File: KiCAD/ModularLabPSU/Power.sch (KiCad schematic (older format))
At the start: 22 parts, among them K1 HF115F, P2 CONN_01X06, Q3 BC847B, Q4 BC847B, U10 LM317_SOT223, U11 LM317AT, U9 LM317HVT

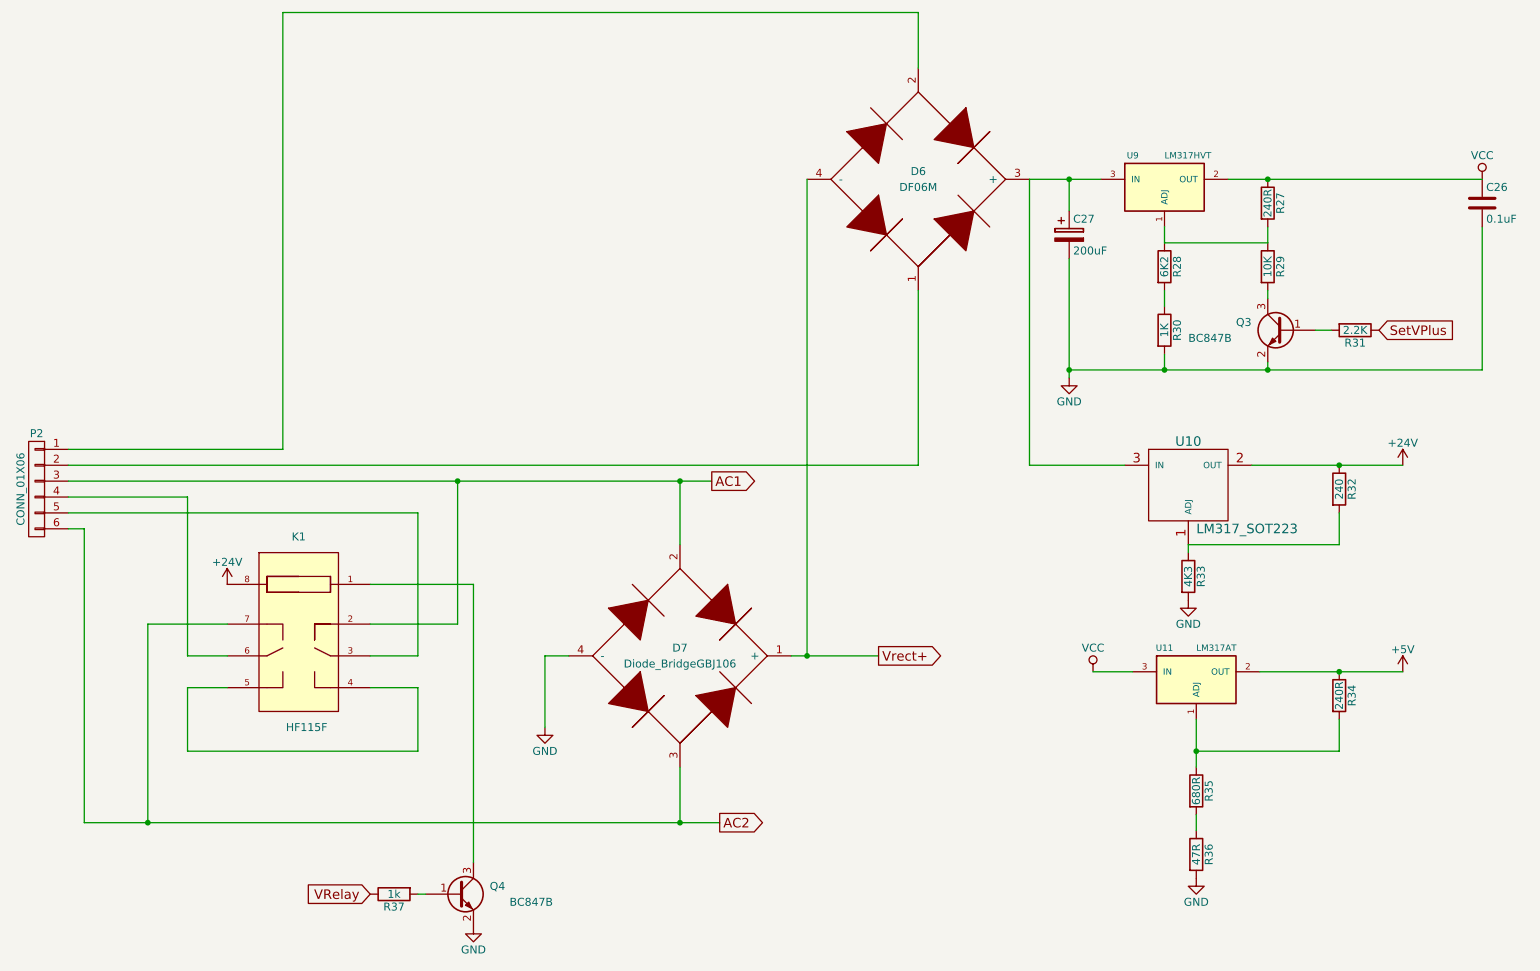
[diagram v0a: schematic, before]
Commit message: Started re-design of PCB. Schematic changes from testing first board and started developing new layout
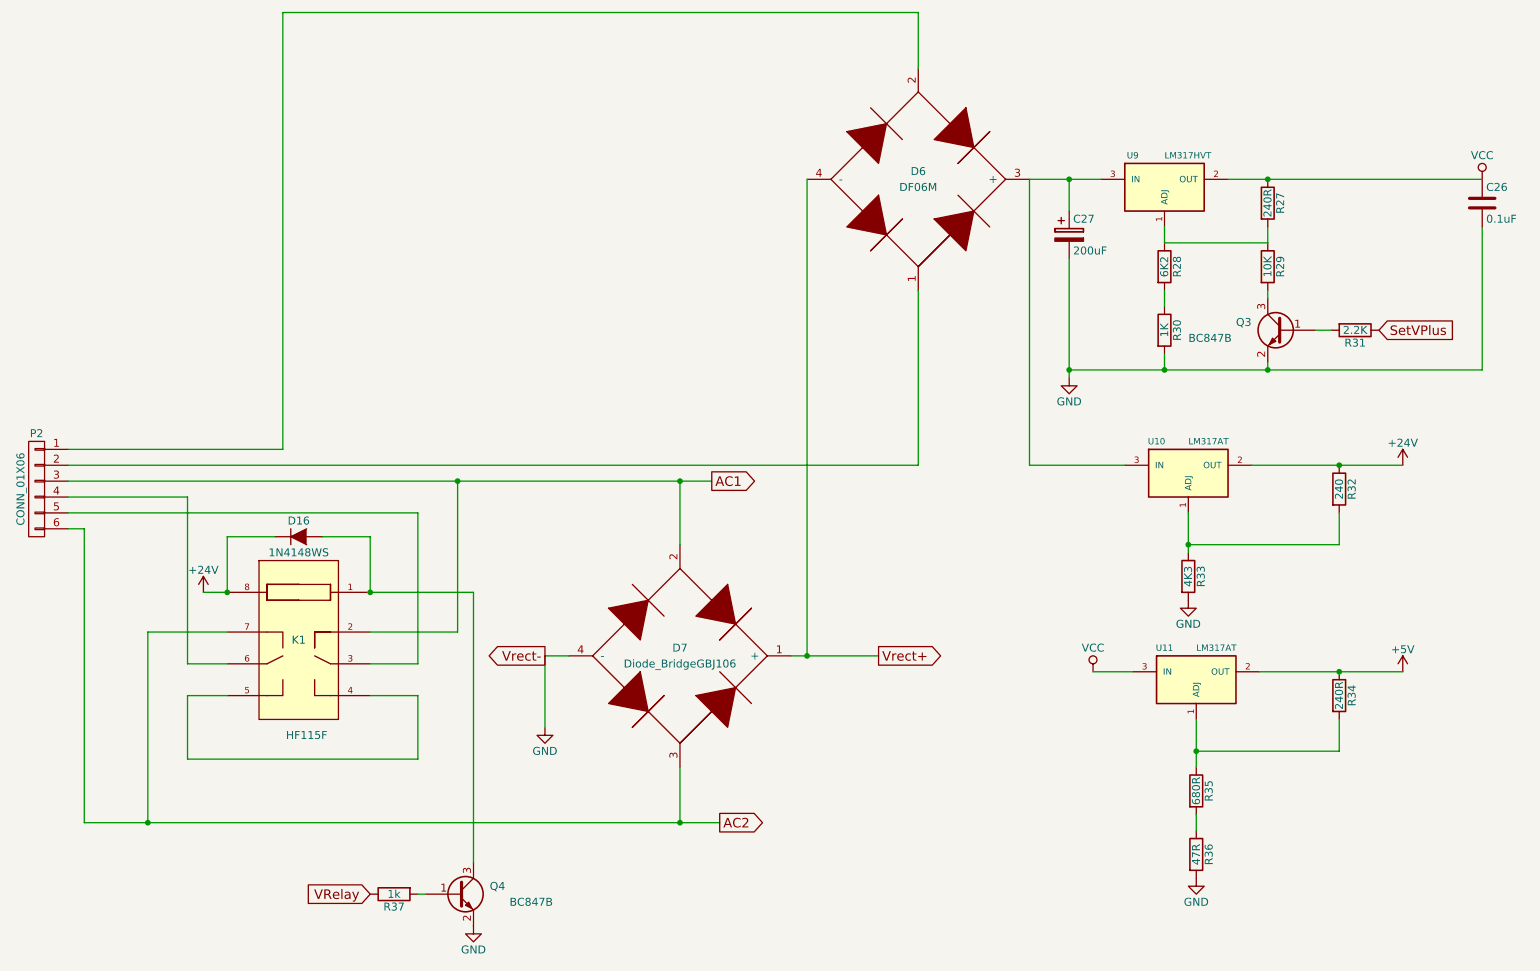
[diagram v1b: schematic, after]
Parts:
- removed U10: LM317_SOT223, ab2_sot:AB2_SOT223, symbol LM317_SOT223
- added D16: 1N4148WS, Diodes_SMD:SOD-323, symbol D
- added U10: LM317AT, Power_Integrations:TO-220, symbol LM317AT
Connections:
- net +24V: now also D16.1 (K), U10.2 (OUT)
- net at C27.1, D6.3 (+), U9.3 (IN): now also U10.3 (IN)
- net at R32.2, R33.1: now also U10.1 (ADJ)
- net at K1.1, Q4.3 (C): now also D16.2 (A)
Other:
- moved on the sheet: K1
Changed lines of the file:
@@
 EESchema Schematic File Version 2
+LIBS:VCS1625
+LIBS:ModularLabPSU-rescue
+LIBS:ceramicResonator
+LIBS:diode_bridge_df06m
+LIBS:diode_bridge_GBJ1506
+LIBS:hf115f
+LIBS:ad780brz
+LIBS:ad5689
+LIBS:ad7705bruz
+LIBS:adum1201arz-rl7
+LIBS:custompower
+LIBS:LM317HVT
+LIBS:LT1639
+LIBS:LT1716
+LIBS:LTC2050
+LIBS:MCP2200
+LIBS:MCR100
+LIBS:MOLEXusb_mini_b_otg
+LIBS:OMRON G2RL-24-CF-DC24
 LIBS:power
 LIBS:device
@@
 LIBS:contrib
 LIBS:valves
-LIBS:ad780brz
-LIBS:ad5689
-LIBS:ad7705bruz
-LIBS:adum1201arz-rl7
-LIBS:ceramicResonator
-LIBS:custompower
-LIBS:diode_bridge_df06m
-LIBS:diode_bridge_GBJ1506
-LIBS:hf115f
-LIBS:LM317HVT
-LIBS:LT1639
-LIBS:LT1716
-LIBS:LTC2050
-LIBS:MCP2200
-LIBS:MCR100
 LIBS:ModularLabPSU-cache
-LIBS:ModularLabPSU-rescue
-LIBS:MOLEXusb_mini_b_otg
-LIBS:OMRON G2RL-24-CF-DC24
 EELAYER 25 0
 EELAYER END
@@
 $EndComp
 $Comp
-L +24V #PWR075
+L +24V #PWR074
 U 1 1 5624A7FF
-P 2400 4350
-F 0 "#PWR075" H 2400 4200 50  0001 C CNN
-F 1 "+24V" H 2400 4490 50  0000 C CNN
-F 2 "" H 2400 4350 60  0000 C CNN
-F 3 "" H 2400 4350 60  0000 C CNN
-	1    2400 4350
+P 2250 4400
+F 0 "#PWR074" H 2250 4250 50  0001 C CNN
+F 1 "+24V" H 2250 4540 50  0000 C CNN
+F 2 "" H 2250 4400 60  0000 C CNN
+F 3 "" H 2250 4400 60  0000 C CNN
+	1    2250 4400
 	1    0    0    -1
 $EndComp
@@
 	1400 3800 2150 3800
 Wire Wire Line
-	2150 3800 2150 4800
-Wire Wire Line
-	2150 4800 2400 4800
-Wire Wire Line
-	1400 3900 3600 3900
-Wire Wire Line
-	3600 3900 3600 4800
-Wire Wire Line
-	3600 4800 3300 4800
-Wire Wire Line
-	2400 5000 2150 5000
-Wire Wire Line
-	2150 5000 2150 5400
-Wire Wire Line
-	2150 5400 3600 5400
-Wire Wire Line
-	3600 5400 3600 5000
-Wire Wire Line
-	3600 5000 3300 5000
-Wire Wire Line
-	2400 4600 1900 4600
-Wire Wire Line
-	1900 4600 1900 5850
+	2150 3800 2150 4850
+Wire Wire Line
+	2150 4850 2400 4850
+Wire Wire Line
+	3600 3900 3600 4850
+Wire Wire Line
+	3600 4850 3300 4850
+Wire Wire Line
+	2400 5050 2150 5050
+Wire Wire Line
+	2150 5450 3600 5450
+Wire Wire Line
+	3600 5450 3600 5050
+Wire Wire Line
+	3600 5050 3300 5050
+Wire Wire Line
+	2400 4650 1900 4650
 Connection ~ 1900 5850
 Wire Wire Line
-	3300 4600 3850 4600
-Wire Wire Line
-	3850 4600 3850 3700
+	3850 4650 3300 4650
+Wire Wire Line
+	3850 3700 3850 4650
 Connection ~ 3850 3700
 $Comp
-L GND #PWR076
+L GND #PWR075
 U 1 1 5624AA06
 P 3950 6500
-F 0 "#PWR076" H 3950 6250 50  0001 C CNN
+F 0 "#PWR075" H 3950 6250 50  0001 C CNN
 F 1 "GND" H 3950 6350 50  0000 C CNN
 F 2 "" H 3950 6500 60  0000 C CNN
@@
 	-1   0    0    -1
 $EndComp
-Wire Wire Line
-	3950 4350 3950 6100
 $Comp
 L R R37
@@
 Connection ~ 5250 5850
 Wire Wire Line
-	3300 4350 3950 4350
+	3300 4400 3950 4400
 Wire Wire Line
 	4550 4800 4400 4800
@@
 	6750 3600 6750 2500
 $Comp
-L GND #PWR077
+L GND #PWR076
 U 1 1 5624D678
 P 4400 5250
-F 0 "#PWR077" H 4400 5000 50  0001 C CNN
+F 0 "#PWR076" H 4400 5000 50  0001 C CNN
 F 1 "GND" H 4400 5100 50  0000 C CNN
 F 2 "" H 4400 5250 60  0000 C CNN
@@
 	7700 2300 7700 3050
 $Comp
-L GND #PWR078
+L GND #PWR077
 U 1 1 5624DFFE
 P 7700 3050
-F 0 "#PWR078" H 7700 2800 50  0001 C CNN
+F 0 "#PWR077" H 7700 2800 50  0001 C CNN
 F 1 "GND" H 7700 2900 50  0000 C CNN
 F 2 "" H 7700 3050 60  0000 C CNN
@@
 	9250 2750 9350 2750
 $Comp
-L VCC #PWR079
+L VCC #PWR078
 U 1 1 5624E69D
 P 10300 1800
-F 0 "#PWR079" H 10300 1650 50  0001 C CNN
+F 0 "#PWR078" H 10300 1650 50  0001 C CNN
 F 1 "VCC" H 10300 1950 50  0000 C CNN
 F 2 "" H 10300 1800 60  0000 C CNN
@@
 	8500 5800 8500 5900
 $Comp
-L GND #PWR080
+L GND #PWR079
 U 1 1 5624F186
 P 8500 6200
-F 0 "#PWR080" H 8500 5950 50  0001 C CNN
+F 0 "#PWR079" H 8500 5950 50  0001 C CNN
 F 1 "GND" H 8500 6050 50  0000 C CNN
 F 2 "" H 8500 6200 60  0000 C CNN
@@
 	7850 4900 8100 4900
 $Comp
-L VCC #PWR081
+L VCC #PWR080
 U 1 1 5624F202
 P 7850 4900
-F 0 "#PWR081" H 7850 4750 50  0001 C CNN
+F 0 "#PWR080" H 7850 4750 50  0001 C CNN
 F 1 "VCC" H 7850 5050 50  0000 C CNN
 F 2 "" H 7850 4900 60  0000 C CNN
@@
 $EndComp
 $Comp
-L +5V #PWR082
+L +5V #PWR081
 U 1 1 5624F229
 P 9800 4900
-F 0 "#PWR082" H 9800 4750 50  0001 C CNN
+F 0 "#PWR081" H 9800 4750 50  0001 C CNN
 F 1 "+5V" H 9800 5040 50  0000 C CNN
 F 2 "" H 9800 4900 60  0000 C CNN
 F 3 "" H 9800 4900 60  0000 C CNN
 	1    9800 4900
-	1    0    0    -1
-$EndComp
-$Comp
-L LM317_SOT223 U10
-U 1 1 5625142C
-P 8450 3750
-F 0 "U10" H 8450 4050 60  0000 C CNN
-F 1 "LM317_SOT223" H 8500 3500 60  0000 L CNN
-F 2 "ab2_sot:AB2_SOT223" H 8450 3750 60  0001 C CNN
-F 3 "" H 8450 3750 60  0000 C CNN
-	1    8450 3750
 	1    0    0    -1
 $EndComp
@@
 	9400 4100 8450 4100
 Wire Wire Line
-	8450 4100 8450 4150
-$Comp
-L GND #PWR083
+	8450 3900 8450 4150
+$Comp
+L GND #PWR082
 U 1 1 56252E95
 P 8450 4450
-F 0 "#PWR083" H 8450 4200 50  0001 C CNN
+F 0 "#PWR082" H 8450 4200 50  0001 C CNN
 F 1 "GND" H 8450 4300 50  0000 C CNN
 F 2 "" H 8450 4450 60  0000 C CNN
@@
 Connection ~ 9400 3600
 $Comp
-L +24V #PWR084
+L +24V #PWR083
 U 1 1 56252F21
 P 9800 3600
-F 0 "#PWR084" H 9800 3450 50  0001 C CNN
+F 0 "#PWR083" H 9800 3450 50  0001 C CNN
 F 1 "+24V" H 9800 3740 50  0000 C CNN
 F 2 "" H 9800 3600 60  0000 C CNN
@@
 L HF115F K1
 U 1 1 562793EF
-P 2850 4650
-F 0 "K1" H 2850 5250 50  0000 C CNN
-F 1 "HF115F" H 2900 4050 50  0000 C CNN
-F 2 "hf115F:HF115F" H 3000 4900 60  0001 C CNN
-F 3 "" H 3000 4900 60  0000 C CNN
-	1    2850 4650
+P 2850 4700
+F 0 "K1" H 2850 4700 50  0000 C CNN
+F 1 "HF115F" H 2900 4100 50  0000 C CNN
+F 2 "hf115F:HF115F" H 3000 4950 60  0001 C CNN
+F 3 "" H 3000 4950 60  0000 C CNN
+	1    2850 4700
 	1    0    0    -1
 $EndComp
@@
 	8900 4900 9800 4900
 Connection ~ 8500 5400
+Wire Wire Line
+	3300 4400 3300 4050
+Wire Wire Line
+	2400 4050 2400 4400
+Wire Wire Line
+	2400 4400 2250 4400
+Connection ~ 2400 4400
+Connection ~ 3300 4400
+$Comp
+L D D16
+U 1 1 5710966E
+P 2850 4050
+F 0 "D16" H 2850 4150 50  0000 C CNN
+F 1 "1N4148WS" H 2850 3950 50  0000 C CNN
+F 2 "Diodes_SMD:SOD-323" H 2850 4050 60  0001 C CNN
+F 3 "" H 2850 4050 60  0000 C CNN
+	1    2850 4050
+	1    0    0    -1
+$EndComp
+Wire Wire Line
+	2700 4050 2400 4050
+Wire Wire Line
+	3300 4050 3000 4050
+Wire Wire Line
+	1400 3900 3600 3900
+Wire Wire Line
+	2150 5050 2150 5450
+Wire Wire Line
+	1900 4650 1900 5850
+Wire Wire Line
+	3950 4400 3950 6100
+$Comp
+L LM317AT U10
+U 1 1 5710AD95
+P 8450 3650
+F 0 "U10" H 8250 3850 40  0000 C CNN
+F 1 "LM317AT" H 8450 3850 40  0000 L CNN
+F 2 "Power_Integrations:TO-220" H 8450 3750 30  0001 C CIN
+F 3 "" H 8450 3650 60  0000 C CNN
+	1    8450 3650
+	1    0    0    -1
+$EndComp
+Connection ~ 8450 4100
+Text GLabel 4400 4800 0    60   Output ~ 0
+Vrect-
 $EndSCHEMATC
